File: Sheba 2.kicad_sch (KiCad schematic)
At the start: 17 parts, among them J1 Conn_01x02_Pin, J2 Conn_02x04_Top_Bottom, J3 Conn_01x06_Pin, P1 USB 2.0 Type-C Port, SW1 SPDT Switch, U1 STM32F072CBTx

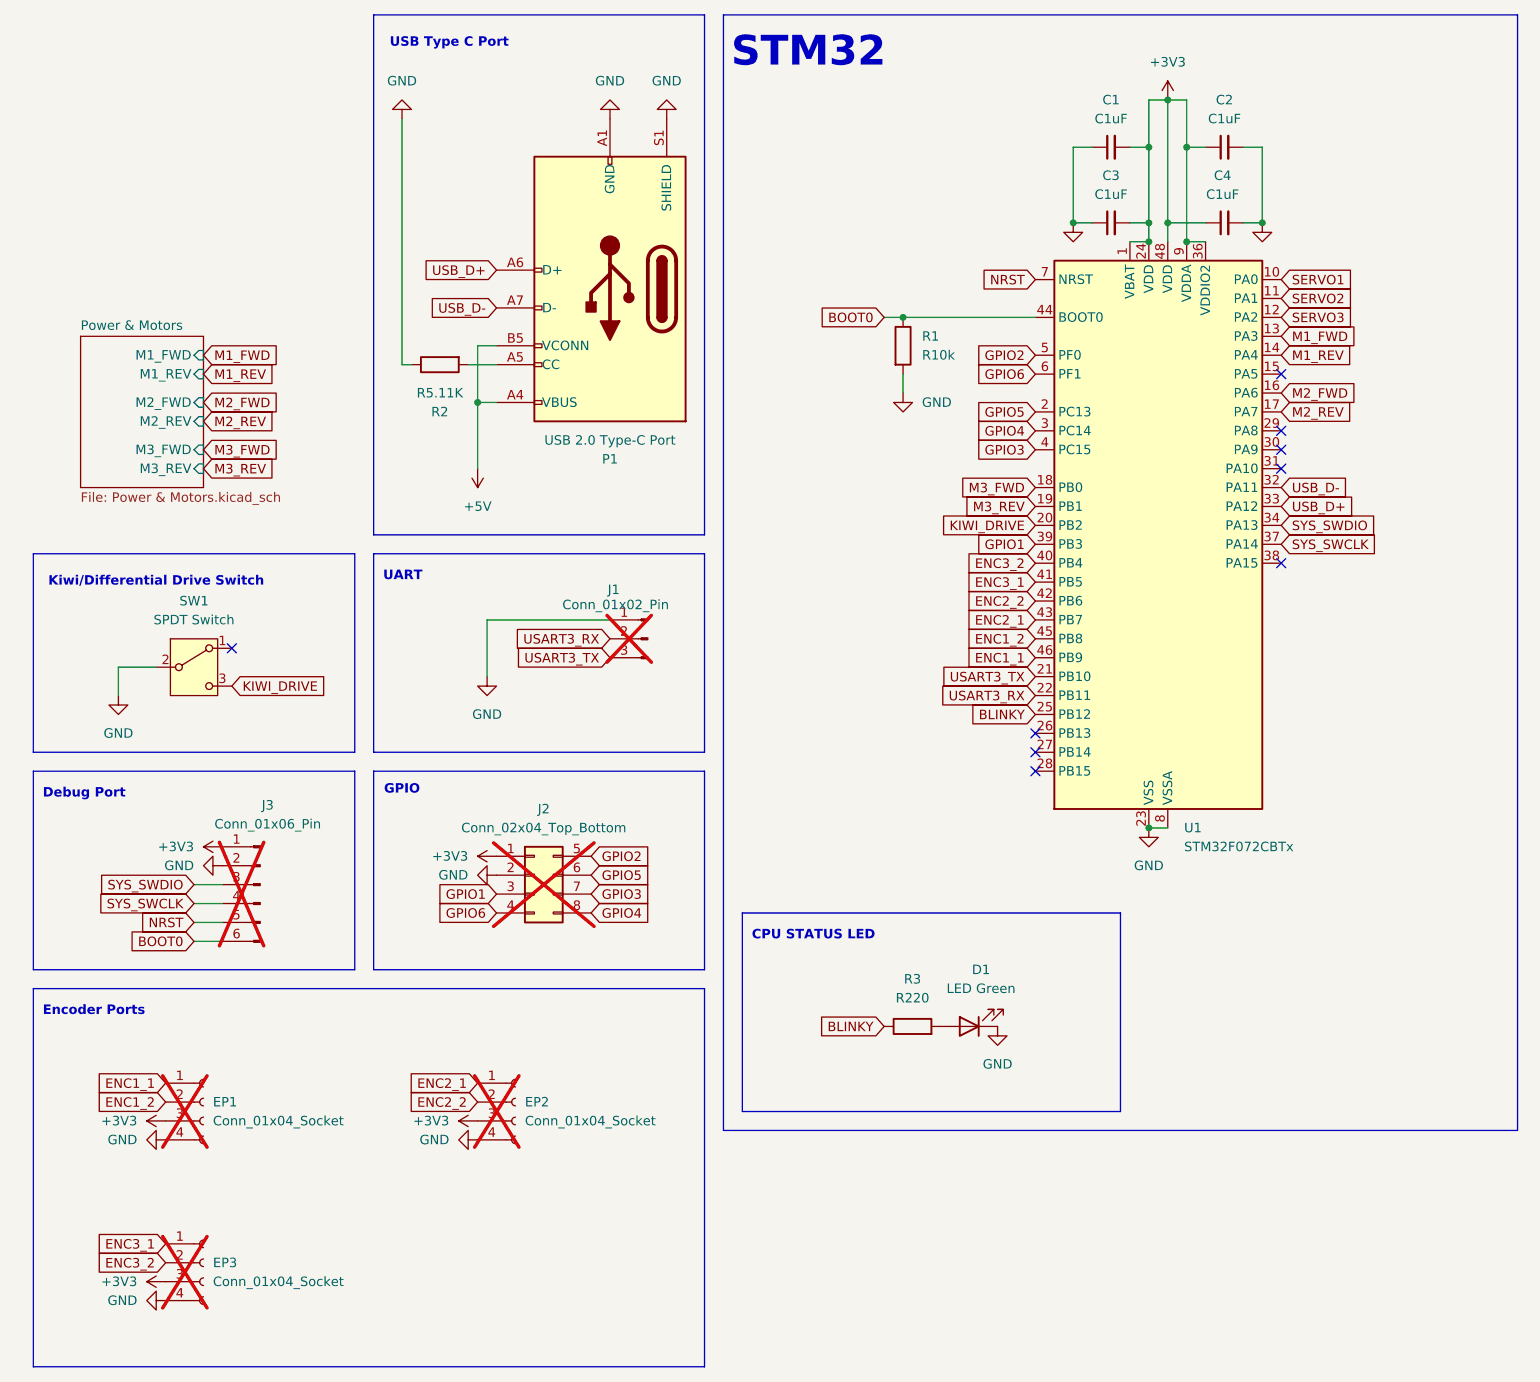
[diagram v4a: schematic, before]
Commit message: change to ESP32-C6-WROOM
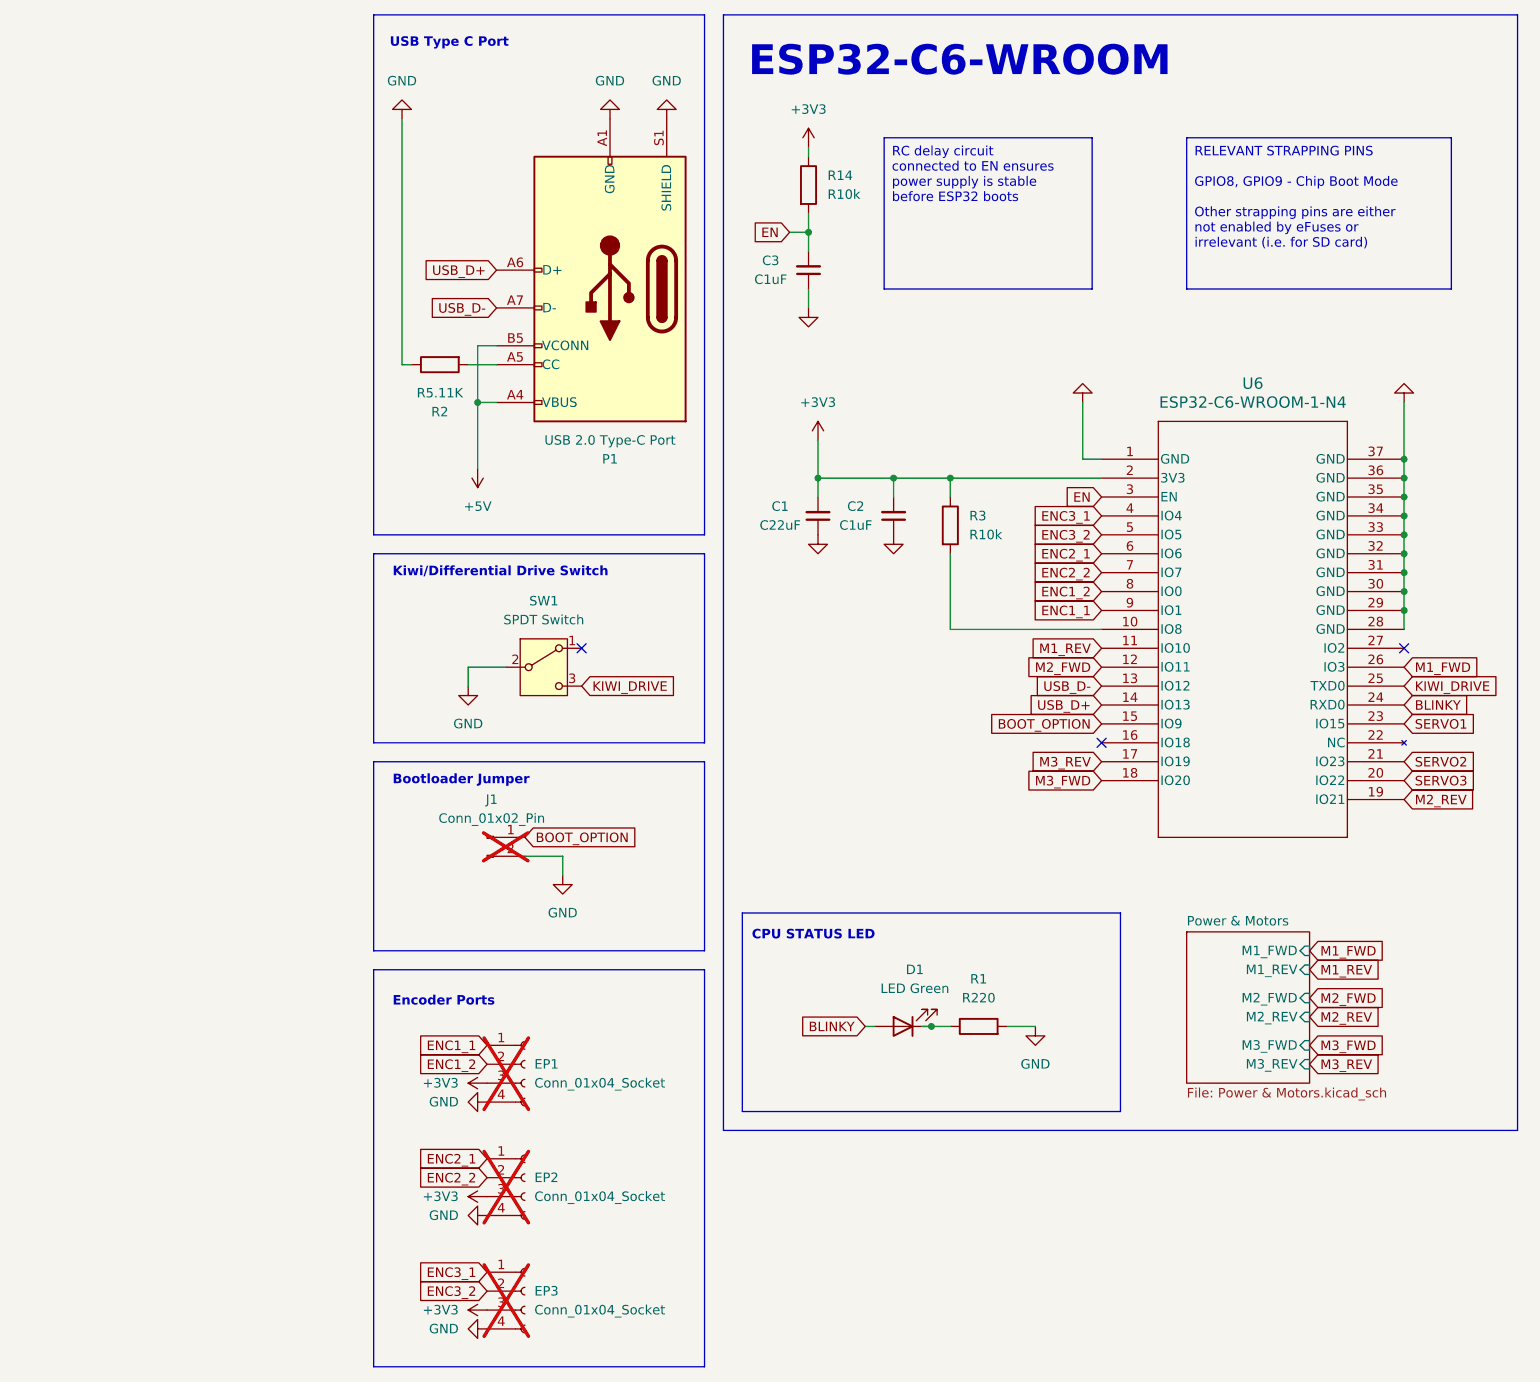
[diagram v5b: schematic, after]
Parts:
- removed C4: C1uF, Capacitor_SMD:C_1206_3216Metric_Pad1.33x1.80mm_HandSolder, symbol Device:C_Small
- removed J1: Conn_01x02_Pin, Connector_PinHeader_2.54mm:PinHeader_1x03_P2.54mm_Vertical, symbol Connector:Conn_01x03_Pin
- removed J2: Conn_02x04_Top_Bottom, Connector_PinSocket_2.54mm:PinSocket_2x04_P2.54mm_Vertical, symbol Connector_Generic:Conn_02x04_Top_Bottom
- removed J3: Conn_01x06_Pin, Connector_PinHeader_2.54mm:PinHeader_1x06_P2.54mm_Vertical, symbol Connector:Conn_01x06_Pin
- removed U1: STM32F072CBTx, Package_QFP:LQFP-48_7x7mm_P0.5mm, symbol MCU_ST_STM32F0:STM32F072CBTx
- added J1: Conn_01x02_Pin, Connector_PinHeader_2.54mm:PinHeader_1x02_P2.54mm_Vertical, symbol Connector:Conn_01x02_Pin
- added R14: R10k, Resistor_SMD:R_1206_3216Metric_Pad1.30x1.75mm_HandSolder, symbol Device:R
- added U6: ESP32-C6-WROOM-1-N4, MOD28_ESP32-C6-WROOM-1_EXP, symbol ESP32-C6-WROOM-1-N4:ESP32-C6-WROOM-1-N4
- C1: value C1uF -> C22uF; DigiKey CL31B105KBHNNNE -> CL31A226MOCLNNC
- R1: value R10k -> R220; DigiKey RC1206FR-0710KL -> RMCF1206JT220R
- R3: value R220 -> R10k; DigiKey RMCF1206JT220R -> RMCF1206FT10K0
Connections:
- net +3V3: now also C2.2, R3.1, R14.1, U6.2 (3V3); no longer C2.1, C3.2
- net BLINKY: now also D1.2 (A), U6.24 (RXD0); no longer R3.1
- net ENC1_1: now also U6.9 (IO1)
- net ENC1_2: now also U6.8 (IO0)
- net ENC2_1: now also U6.6 (IO6)
- net ENC2_2: now also U6.7 (IO7)
- net ENC3_1: now also U6.4 (IO4)
- net ENC3_2: now also U6.5 (IO5)
- net GND: now also C2.1, J1.2 (Pin_2), U6.1 (GND), U6.28 (GND), U6.29 (GND), U6.30 (GND), U6.31 (GND), U6.32 (GND), U6.33 (GND), U6.34 (GND), U6.35 (GND), U6.36 (GND), U6.37 (GND); no longer C2.2, D1.1 (K)
- net KIWI_DRIVE: now also U6.25 (TXD0)
- net M1_FWD: now also U6.26 (IO3)
- net M1_REV: now also U6.11 (IO10)
- net M2_FWD: now also U6.12 (IO11)
- net M2_REV: now also U6.19 (IO21)
- net M3_FWD: now also U6.18 (IO20)
- net M3_REV: now also U6.17 (IO19)
- net SERVO1: now also U6.23 (IO15)
- net SERVO2: now also U6.21 (IO23)
- net SERVO3: now also U6.20 (IO22)
- net USB_D+: now also U6.14 (IO13)
- net USB_D-: now also U6.13 (IO12)
- net at R3.2: now also U6.10 (IO8); no longer D1.2 (A)
- net BOOT0: no longer names the net of R1.1
- net BOOT0: now also D1.1 (K)
- new net BOOT_OPTION: J1.1 (Pin_1), U6.15 (IO9)
- new net EN: C3.2, R14.2, U6.3 (EN)
- no-connect marks 9 -> 3
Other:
- note added: "Bootloader Jumper"
- note added: "ESP32-C6-WROOM"
- note removed: "Debug Port"
- note removed: "GPIO"
- note removed: "STM32"
- note removed: "UART"
- moved on the sheet: EP1, EP2, EP3, SW1

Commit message: i forgor
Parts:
- C1: value C22uF -> 22uF
- C2, C3: value C1uF -> 1uF
- R1: value R220 -> 220
- R14, R3: value R10k -> 10k
- R2: value R5.11K -> 5.11k
- SW1: now not fitted
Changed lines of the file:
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@@
 		(in_bom yes)
 		(on_board yes)
-		(dnp no)
+		(dnp yes)
 		(fields_autoplaced yes)
 		(property "Reference" "SW1"
@@
 			)
 		)
-		(property "Value" "R5.11K"
+		(property "Value" "5.11k"
 			(at 138.43 64.77 90)
 			(effects
@@
 			)
 		)
-		(property "Value" "C22uF"
+		(property "Value" "22uF"
 			(at 184.1563 82.55 0)
 			(effects
@@
 			)
 		)
-		(property "Value" "C1uF"
+		(property "Value" "1uF"
 			(at 194.3163 82.55 0)
 			(effects
@@
 			)
 		)
-		(property "Value" "R10k"
+		(property "Value" "10k"
 			(at 190.5 38.0999 0)
 			(effects
@@
 			)
 		)
-		(property "Value" "R10k"
+		(property "Value" "10k"
 			(at 209.55 83.8199 0)
 			(effects
@@
 			)
 		)
-		(property "Value" "C1uF"
+		(property "Value" "1uF"
 			(at 182.8863 49.53 0)
 			(effects
@@
 			)
 		)
-		(property "Value" "R220"
+		(property "Value" "220"
 			(at 210.82 146.05 90)
 			(effects
